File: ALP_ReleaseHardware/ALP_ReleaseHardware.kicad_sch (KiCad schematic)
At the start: 45 parts

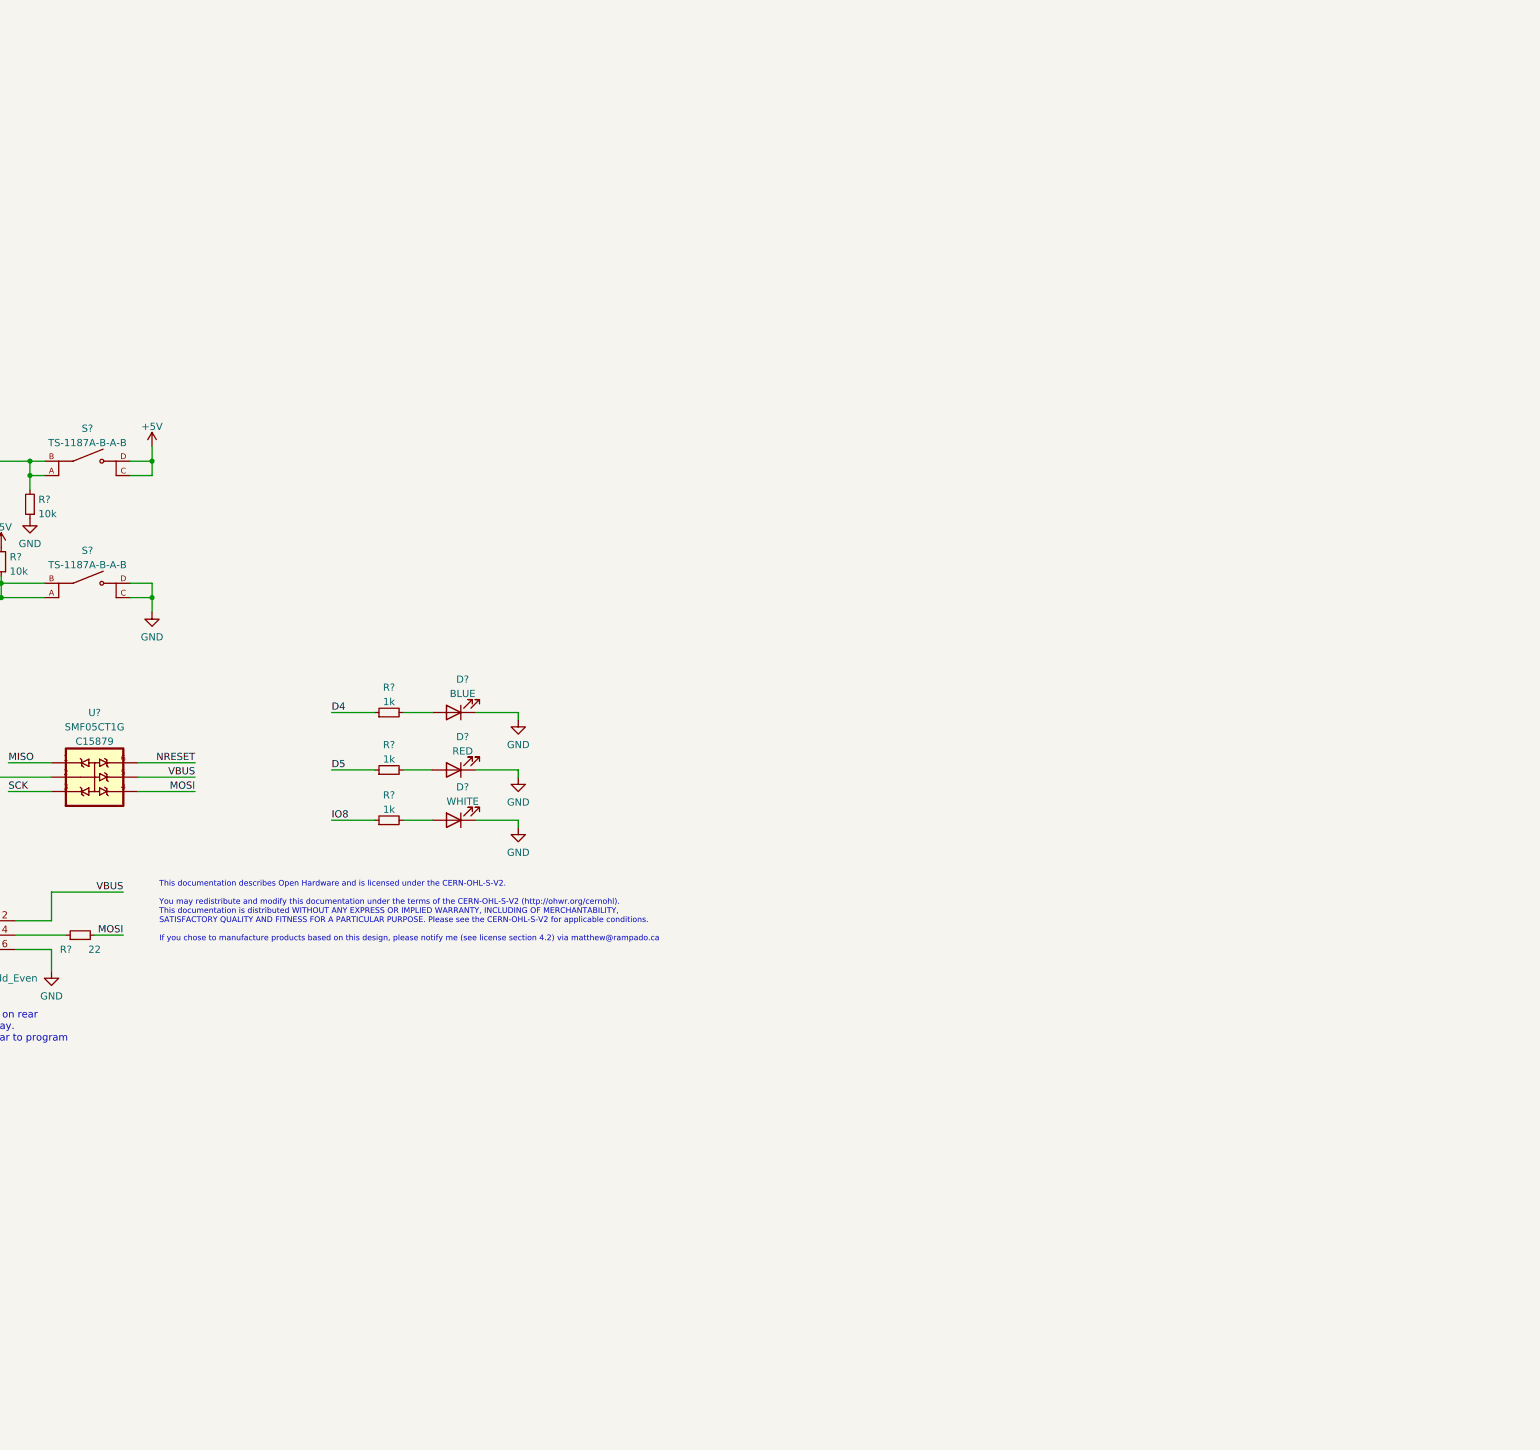
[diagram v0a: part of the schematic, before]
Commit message: Added Side LEDs to go on bottom
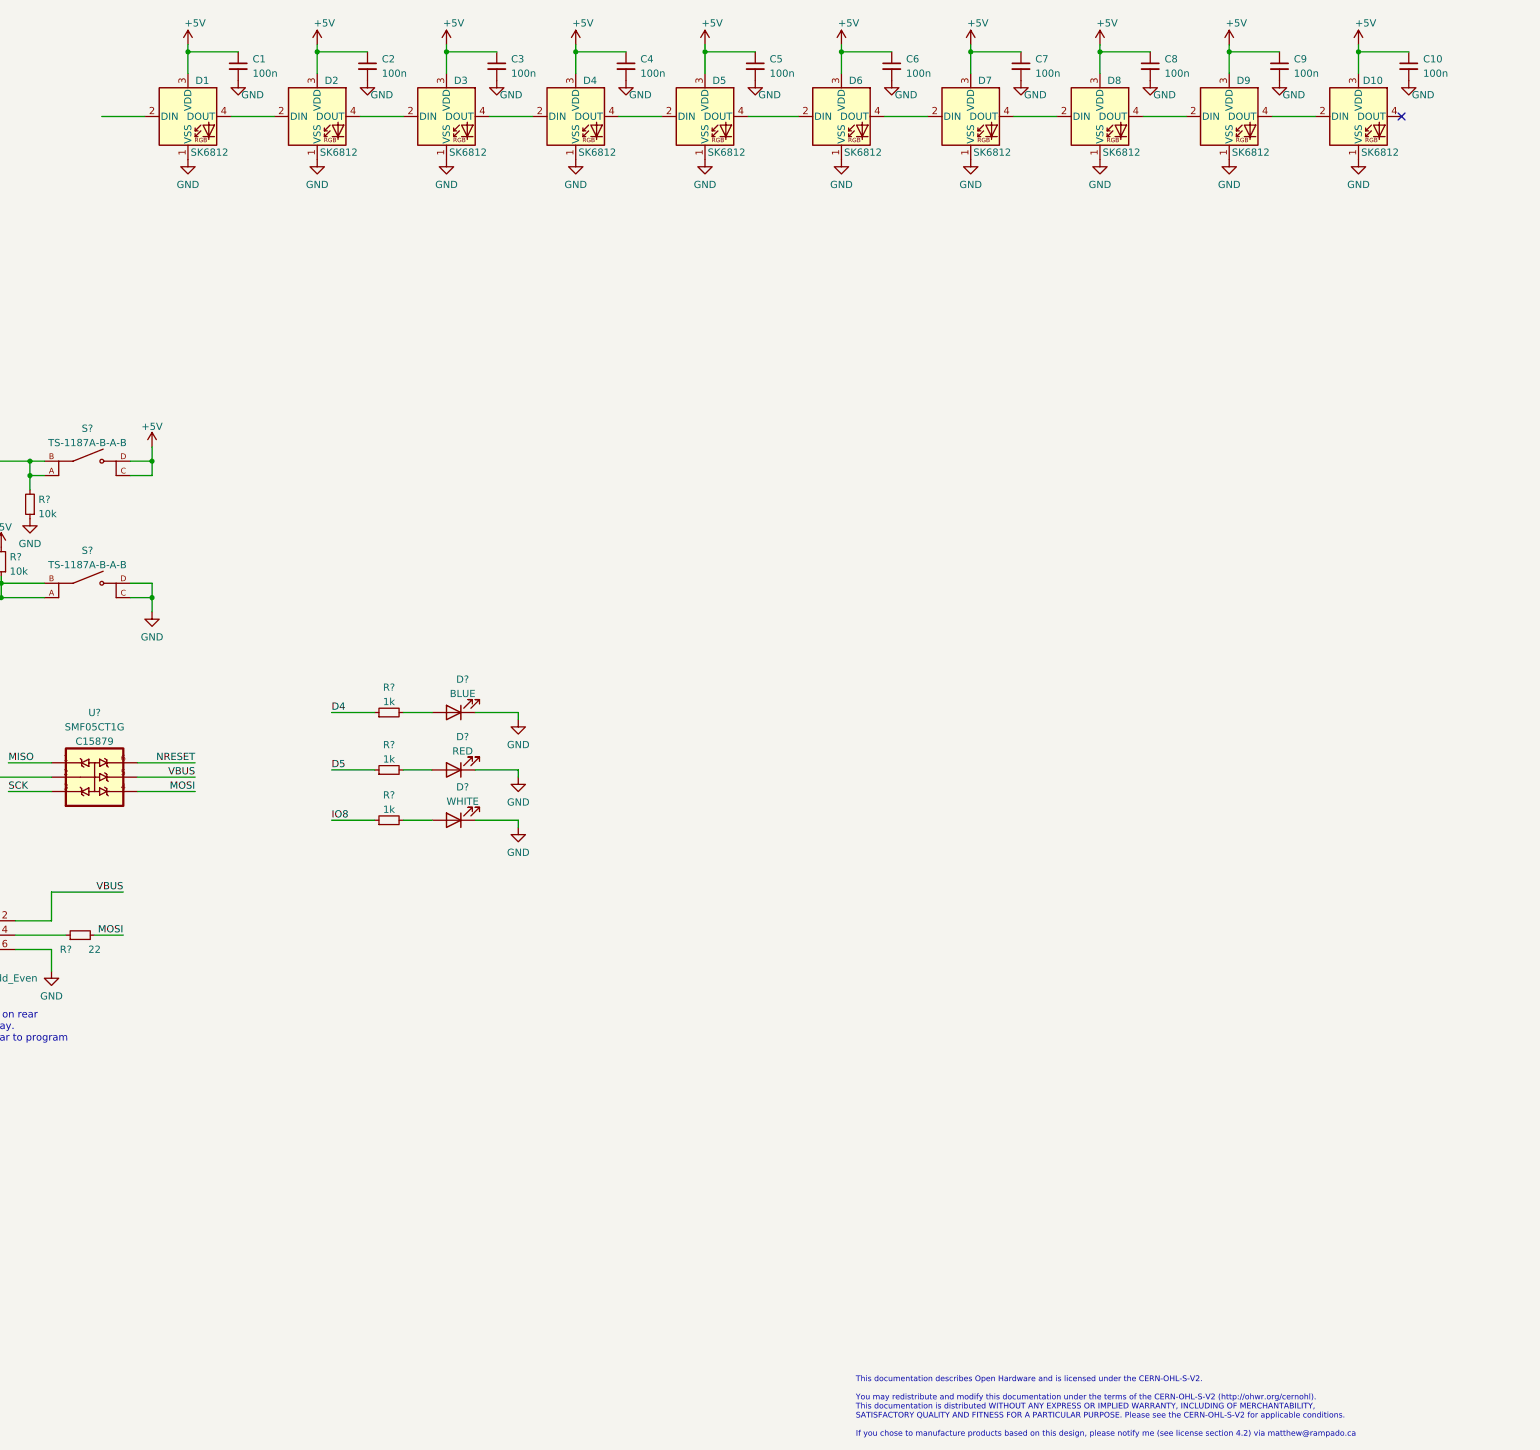
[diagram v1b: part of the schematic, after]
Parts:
- added C1, C10, C2, C3, C4, C5, C6, C7, C8, C9: 100n, symbol Device:C_Small
- added D1, D10, D2, D3, D4, D5, D6, D7, D8, D9: SK6812, symbol Rampado_Master:SK6812_Side
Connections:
- net +5V: now also C1.1, C10.1, C2.1, C3.1, C4.1, C5.1, C6.1, C7.1, C8.1, C9.1, D1.3 (VDD), D10.3 (VDD), D2.3 (VDD), D3.3 (VDD), D4.3 (VDD), D5.3 (VDD), D6.3 (VDD), D7.3 (VDD), D8.3 (VDD), D9.3 (VDD)
- net GND: now also C1.2, C10.2, C2.2, C3.2, C4.2, C5.2, C6.2, C7.2, C8.2, C9.2, D1.1 (VSS), D10.1 (VSS), D2.1 (VSS), D3.1 (VSS), D4.1 (VSS), D5.1 (VSS), D6.1 (VSS), D7.1 (VSS), D8.1 (VSS), D9.1 (VSS)
- new net: D3.4 (DOUT), D4.2 (DIN)
- new net: D4.4 (DOUT), D5.2 (DIN)
- new net: D1.4 (DOUT), D2.2 (DIN)
- new net: D2.4 (DOUT), D3.2 (DIN)
- new net: D5.4 (DOUT), D6.2 (DIN)
- new net: D10.2 (DIN), D9.4 (DOUT)
- new net: D6.4 (DOUT), D7.2 (DIN)
- new net: D8.4 (DOUT), D9.2 (DIN)
- new net: D7.4 (DOUT), D8.2 (DIN)
- no-connect marks 12 -> 13
